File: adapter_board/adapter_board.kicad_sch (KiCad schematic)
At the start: 19 parts, among them J1 Conn_01x05_Female, J10 Conn_01x04_Female, J11 Conn_01x04_Female, J12 Conn_01x04_Female, J13 Conn_01x04_Female, J14 Conn_01x04_Female, J2 Conn_01x12_Female, J3 Conn_01x04_Female, J4 Conn_01x02_Female, J5 Conn_01x05_Female, J6 Conn_01x04_Female, J7 Conn_01x06_Female, J8 Conn_01x06_Female, J9 Conn_01x04_Female, U1 PC104

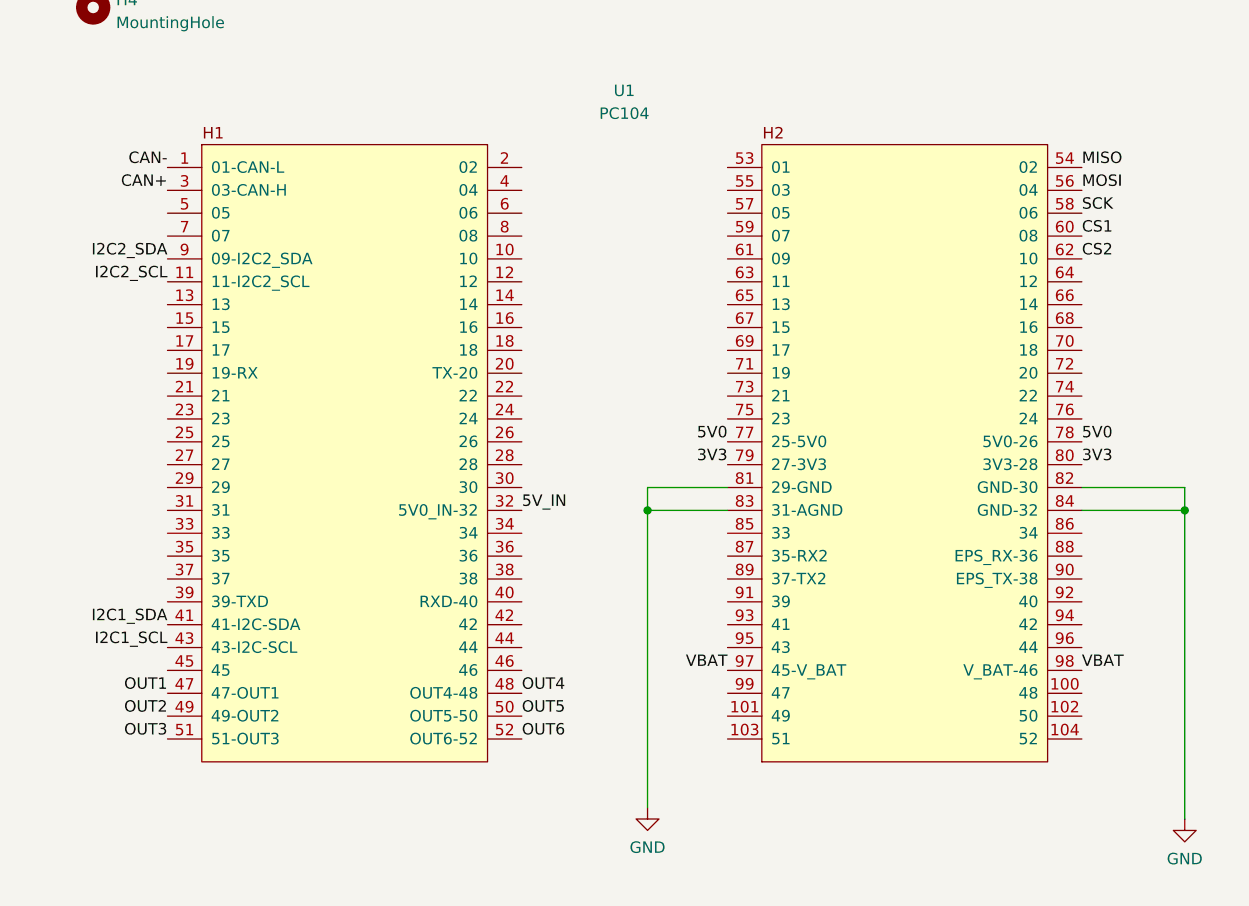
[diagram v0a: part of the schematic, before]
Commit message: added labels to and generated gerber for adapter board
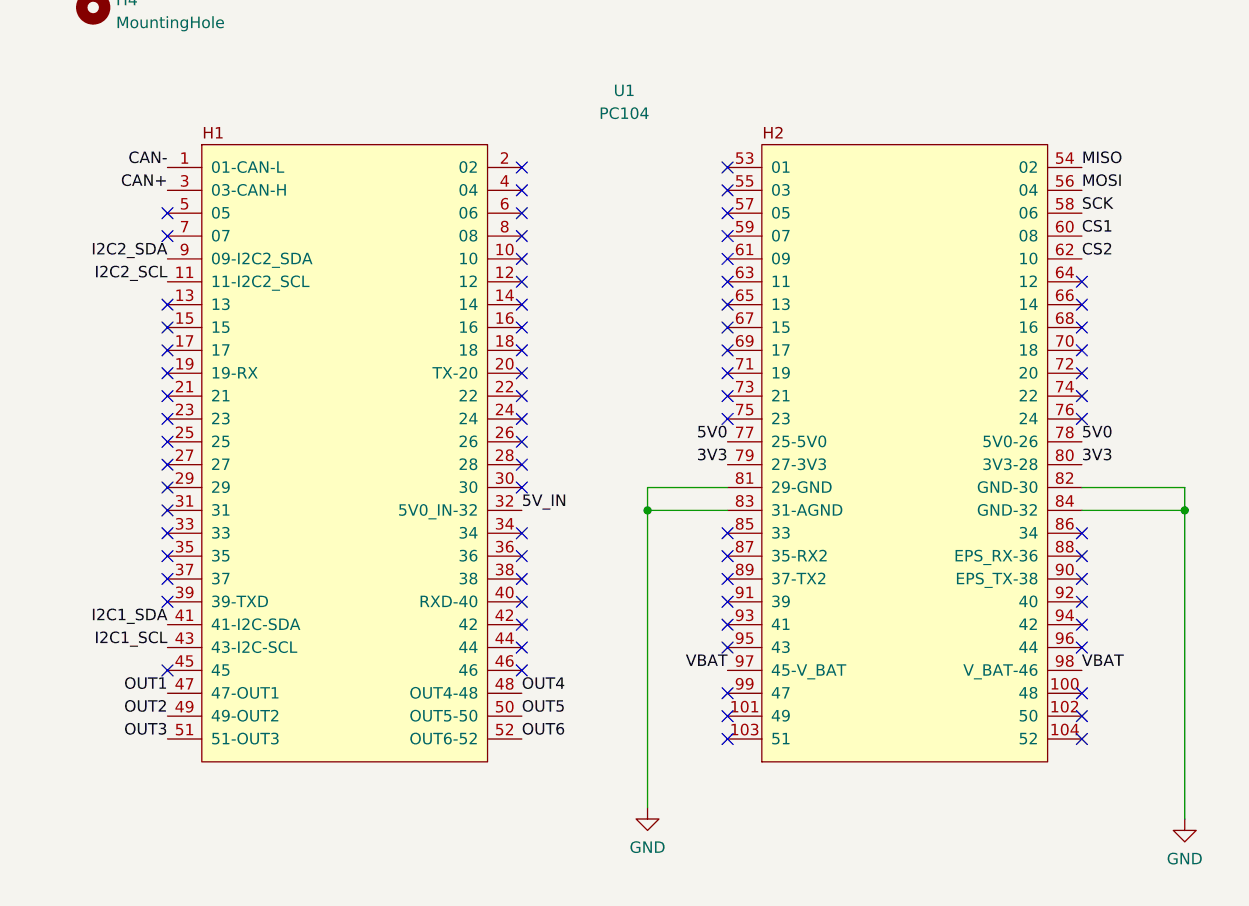
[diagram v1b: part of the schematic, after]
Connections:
- no-connect marks 0 -> 76
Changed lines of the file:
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@@
   (junction (at 209.55 100.33) (diameter 0) (color 0 0 0 0)
   )
+  (no_connect (at 198.12 102.87))
+  (no_connect (at 198.12 74.93))
+  (no_connect (at 198.12 77.47))
+  (no_connect (at 198.12 80.01))
+  (no_connect (at 198.12 82.55))
+  (no_connect (at 198.12 85.09))
+  (no_connect (at 198.12 87.63))
+  (no_connect (at 198.12 90.17))
+  (no_connect (at 198.12 120.65))
+  (no_connect (at 198.12 123.19))
+  (no_connect (at 198.12 125.73))
+  (no_connect (at 198.12 105.41))
+  (no_connect (at 198.12 107.95))
+  (no_connect (at 198.12 110.49))
+  (no_connect (at 198.12 113.03))
+  (no_connect (at 198.12 115.57))
+  (no_connect (at 158.75 125.73))
+  (no_connect (at 158.75 102.87))
+  (no_connect (at 158.75 105.41))
+  (no_connect (at 158.75 107.95))
+  (no_connect (at 158.75 110.49))
+  (no_connect (at 158.75 113.03))
+  (no_connect (at 158.75 115.57))
+  (no_connect (at 158.75 120.65))
+  (no_connect (at 158.75 123.19))
+  (no_connect (at 158.75 87.63))
+  (no_connect (at 158.75 90.17))
+  (no_connect (at 158.75 64.77))
+  (no_connect (at 158.75 67.31))
+  (no_connect (at 158.75 69.85))
+  (no_connect (at 158.75 72.39))
+  (no_connect (at 158.75 74.93))
+  (no_connect (at 158.75 77.47))
+  (no_connect (at 158.75 80.01))
+  (no_connect (at 158.75 82.55))
+  (no_connect (at 158.75 85.09))
+  (no_connect (at 135.89 118.11))
+  (no_connect (at 135.89 115.57))
+  (no_connect (at 135.89 113.03))
+  (no_connect (at 135.89 110.49))
+  (no_connect (at 135.89 107.95))
+  (no_connect (at 135.89 105.41))
+  (no_connect (at 135.89 102.87))
+  (no_connect (at 135.89 97.79))
+  (no_connect (at 135.89 95.25))
+  (no_connect (at 135.89 92.71))
+  (no_connect (at 135.89 90.17))
+  (no_connect (at 135.89 87.63))
+  (no_connect (at 96.52 77.47))
+  (no_connect (at 96.52 80.01))
+  (no_connect (at 96.52 82.55))
+  (no_connect (at 96.52 85.09))
+  (no_connect (at 96.52 67.31))
+  (no_connect (at 96.52 69.85))
+  (no_connect (at 96.52 87.63))
+  (no_connect (at 96.52 90.17))
+  (no_connect (at 96.52 105.41))
+  (no_connect (at 96.52 107.95))
+  (no_connect (at 96.52 110.49))
+  (no_connect (at 96.52 118.11))
+  (no_connect (at 96.52 92.71))
+  (no_connect (at 96.52 95.25))
+  (no_connect (at 96.52 97.79))
+  (no_connect (at 96.52 100.33))
+  (no_connect (at 96.52 102.87))
+  (no_connect (at 135.89 85.09))
+  (no_connect (at 135.89 82.55))
+  (no_connect (at 135.89 80.01))
+  (no_connect (at 135.89 77.47))
+  (no_connect (at 135.89 74.93))
+  (no_connect (at 135.89 72.39))
+  (no_connect (at 135.89 69.85))
+  (no_connect (at 135.89 67.31))
+  (no_connect (at 135.89 64.77))
+  (no_connect (at 135.89 62.23))
+  (no_connect (at 158.75 62.23))
   (wire (pts (xy 209.55 134.62) (xy 209.55 100.33))
     (stroke (width 0) (type default) (color 0 0 0 0))
